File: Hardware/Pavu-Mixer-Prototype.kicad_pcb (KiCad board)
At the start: 2 copper layers, 155.9 x 91.9 mm, 65 parts, among them J1 Conn_02x16_Counter_Clockwise, U1 74HC595, U2 74HC595, U3 74HC595, U4 PCA9555D, U5 PCA9536D

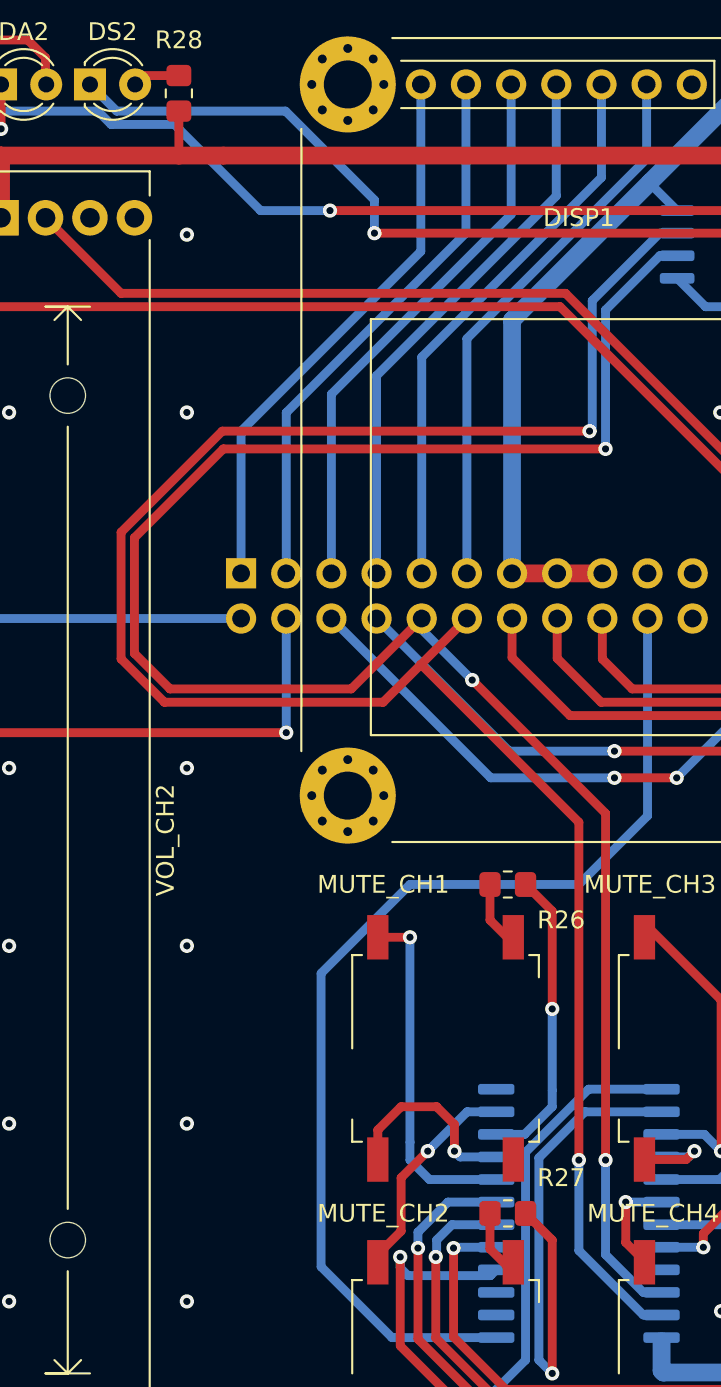
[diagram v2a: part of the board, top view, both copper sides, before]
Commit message: Cleanup some tracks
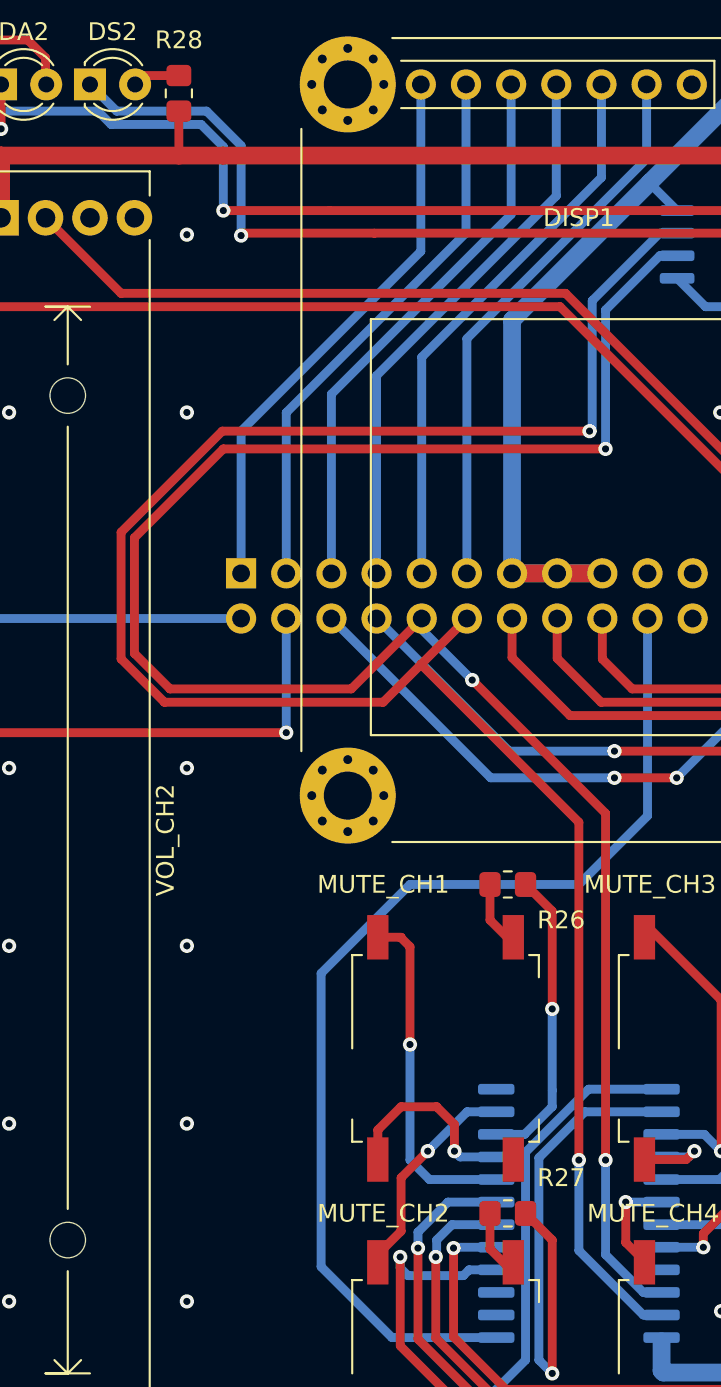
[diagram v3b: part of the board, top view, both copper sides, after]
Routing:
- net +3V3: track 456.7 -> 462.0 mm
- net /DESYNC_CH1: track 60.3 -> 62.4 mm
- net /DESYNC_CH2: track 46.6 -> 48.6 mm
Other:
- board text added: "Pavu-Mixer Rev 1.0 2021-03-29 Rahix"
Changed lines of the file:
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@@
   (general
     (thickness 1.6)
-    (drawings 6)
-    (tracks 642)
+    (drawings 7)
+    (tracks 649)
     (zones 0)
     (modules 65)
@@
     (tags "SOIC SO")
     (attr smd)
-    (fp_text reference U5 (at 0 3.4) (layer B.SilkS)
+    (fp_text reference U5 (at 0 3.5) (layer B.SilkS)
       (effects (font (size 1 1) (thickness 0.15)) (justify mirror))
     )
@@
     (tags "SOIC SO")
     (attr smd)
-    (fp_text reference U4 (at 0 8.65) (layer B.SilkS)
+    (fp_text reference U4 (at 0.5 9) (layer B.SilkS)
       (effects (font (size 1 1) (thickness 0.15)) (justify mirror))
     )
@@
     (tags "SOIC SO")
     (attr smd)
-    (fp_text reference U3 (at 0 5.9) (layer B.SilkS)
+    (fp_text reference U3 (at 1.5 6) (layer B.SilkS)
       (effects (font (size 1 1) (thickness 0.15)) (justify mirror))
     )
@@
     (tags "SOIC SO")
     (attr smd)
-    (fp_text reference U2 (at 0 5.9) (layer B.SilkS)
+    (fp_text reference U2 (at 1.5 6) (layer B.SilkS)
       (effects (font (size 1 1) (thickness 0.15)) (justify mirror))
     )
@@
     (tags "SOIC SO")
     (attr smd)
-    (fp_text reference U1 (at 0 5.9) (layer B.SilkS)
+    (fp_text reference U1 (at 1.5 6) (layer B.SilkS)
       (effects (font (size 1 1) (thickness 0.15)) (justify mirror))
     )
@@
     (descr "Through hole straight pin header, 2x16, 2.54mm pitch, double rows")
     (tags "Through hole pin header THT 2x16 2.54mm double row")
-    (fp_text reference J1 (at 1.27 2.33 90) (layer B.SilkS)
+    (fp_text reference J1 (at 0 3 180) (layer B.SilkS)
       (effects (font (size 1 1) (thickness 0.15)) (justify mirror))
     )
@@
     )
   )
+  (gr_text "Pavu-Mixer Rev 1.0\n2021-03-29  Rahix" (at 92.5 106) (layer B.SilkS)
+    (effects (font (size 2 2) (thickness 0.15)) (justify mirror))
+  )
   (dimension 155.9 (width 0.15) (layer Dwgs.User)
     (gr_text "155.900 mm" (at 147.95 152.2) (layer Dwgs.User)
@@
   (segment (start 159.05 120.4) (end 144.5 134.95) (width 1) (layer B.Cu) (net 52))
   (segment (start 180.5 120.4) (end 159.05 120.4) (width 1) (layer B.Cu) (net 52))
+  (segment (start 126.24 90) (end 131.5 90) (width 1) (layer B.Cu) (net 52))
   (segment (start 126.19 69.81) (end 126.19 62.5) (width 0.5) (layer B.Cu) (net 53))
   (segment (start 116.08 79.92) (end 126.19 69.81) (width 0.5) (layer B.Cu) (net 53))
@@
   (via (at 142.5 69.595) (size 0.8) (drill 0.4) (layers F.Cu B.Cu) (net 58))
   (segment (start 142.5 69.595) (end 116 69.595) (width 0.5) (layer F.Cu) (net 58))
-  (via (at 116 69.595) (size 0.8) (drill 0.4) (layers F.Cu B.Cu) (net 58))
-  (segment (start 112.095 69.595) (end 116 69.595) (width 0.5) (layer B.Cu) (net 58))
-  (segment (start 107.25001 64.75001) (end 112.095 69.595) (width 0.5) (layer B.Cu) (net 58))
+  (segment (start 116 69.595) (end 110 69.595) (width 0.5) (layer F.Cu) (net 58))
+  (via (at 110 69.595) (size 0.8) (drill 0.4) (layers F.Cu B.Cu) (net 58))
+  (segment (start 108.75001 64.75001) (end 110 66) (width 0.5) (layer B.Cu) (net 58))
+  (segment (start 110 66) (end 110 69.595) (width 0.5) (layer B.Cu) (net 58))
+  (segment (start 103.689336 64.75001) (end 108.75001 64.75001) (width 0.5) (layer B.Cu) (net 58))
   (segment (start 102.939326 64) (end 103.689336 64.75001) (width 0.5) (layer B.Cu) (net 58))
   (segment (start 88.5 64) (end 102.939326 64) (width 0.5) (layer B.Cu) (net 58))
   (segment (start 87.5 63) (end 88.5 64) (width 0.5) (layer B.Cu) (net 58))
-  (segment (start 103.689336 64.75001) (end 107.25001 64.75001) (width 0.5) (layer B.Cu) (net 58))
   (segment (start 87.5 62.5) (end 87.5 63) (width 0.5) (layer B.Cu) (net 58))
   (segment (start 105.5 62) (end 105 62.5) (width 0.5) (layer F.Cu) (net 59))
@@
   (via (at 142.5 70.865) (size 0.8) (drill 0.4) (layers F.Cu B.Cu) (net 60))
   (segment (start 142.5 70.865) (end 118.5 70.865) (width 0.5) (layer F.Cu) (net 60))
-  (via (at 118.5 70.865) (size 0.8) (drill 0.4) (layers F.Cu B.Cu) (net 60))
-  (segment (start 118.5 70.865) (end 118.5 69) (width 0.5) (layer B.Cu) (net 60))
-  (segment (start 118.5 69) (end 113.5 64) (width 0.5) (layer B.Cu) (net 60))
-  (segment (start 113.5 64) (end 104 64) (width 0.5) (layer B.Cu) (net 60))
   (segment (start 104 64) (end 102.5 62.5) (width 0.5) (layer B.Cu) (net 60))
+  (segment (start 109.060675 64.000001) (end 111 65.939326) (width 0.5) (layer B.Cu) (net 60))
+  (segment (start 104 64) (end 109.060675 64.000001) (width 0.5) (layer B.Cu) (net 60))
+  (via (at 111 71) (size 0.8) (drill 0.4) (layers F.Cu B.Cu) (net 60))
+  (segment (start 111.135 70.865) (end 111 71) (width 0.5) (layer F.Cu) (net 60))
+  (segment (start 118.5 70.865) (end 111.135 70.865) (width 0.5) (layer F.Cu) (net 60))
+  (segment (start 111 71) (end 111 65.939326) (width 0.5) (layer B.Cu) (net 60))
   (segment (start 165 62) (end 163 62) (width 0.5) (layer F.Cu) (net 61))
   (segment (start 163 62) (end 162.5 62.5) (width 0.5) (layer F.Cu) (net 61))
@@
   (via (at 119.95 128.45) (size 0.8) (drill 0.4) (layers F.Cu B.Cu) (net 66))
   (segment (start 119.949997 129.065685) (end 120.384312 129.5) (width 0.5) (layer B.Cu) (net 66))
-  (segment (start 125.025 129.5) (end 120.384312 129.5) (width 0.5) (layer B.Cu) (net 66))
-  (segment (start 125.35 129.175) (end 125.025 129.5) (width 0.5) (layer B.Cu) (net 66))
   (segment (start 147.9 138.5) (end 147.95 138.45) (width 0.5) (layer F.Cu) (net 66))
   (segment (start 120 133.5) (end 125 138.5) (width 0.5) (layer F.Cu) (net 66))
@@
   (segment (start 119.949997 129.065685) (end 119.949997 128.450003) (width 0.5) (layer B.Cu) (net 66))
   (segment (start 119.95 128.45) (end 119.95 133.45) (width 0.5) (layer F.Cu) (net 66))
+  (segment (start 125.35 129.175) (end 123.825 129.175) (width 0.5) (layer B.Cu) (net 66))
+  (segment (start 123.5 129.5) (end 120.384312 129.5) (width 0.5) (layer B.Cu) (net 66))
+  (segment (start 123.825 129.175) (end 123.5 129.5) (width 0.5) (layer B.Cu) (net 66))
   (segment (start 134.55 72.135) (end 131.5 75.185) (width 0.5) (layer B.Cu) (net 67))
   (segment (start 135.525 72.135) (end 134.55 72.135) (width 0.5) (layer B.Cu) (net 67))
@@
   (segment (start 123.325 122.825) (end 123 122.5) (width 0.5) (layer B.Cu) (net 78))
   (segment (start 125.35 122.825) (end 123.325 122.825) (width 0.5) (layer B.Cu) (net 78))
-  (segment (start 118.69 110.469) (end 120.5 110.469) (width 0.5) (layer F.Cu) (net 79))
-  (via (at 120.5 110.469) (size 0.8) (drill 0.4) (layers F.Cu B.Cu) (net 79))
-  (segment (start 120.5 110.469) (end 120.5 122) (width 0.5) (layer B.Cu) (net 79))
-  (segment (start 125.35 124.095) (end 121.595 124.095) (width 0.5) (layer B.Cu) (net 79))
-  (segment (start 120.5 123) (end 120.5 122) (width 0.5) (layer B.Cu) (net 79))
-  (segment (start 121.595 124.095) (end 120.5 123) (width 0.5) (layer B.Cu) (net 79))
+  (segment (start 118.69 110.469) (end 120 110.469) (width 0.5) (layer F.Cu) (net 79))
+  (segment (start 120 110.469) (end 120 110.5) (width 0.5) (layer F.Cu) (net 79))
+  (segment (start 120 110.5) (end 120.5 111) (width 0.5) (layer F.Cu) (net 79))
+  (segment (start 120.5 111) (end 120.5 116.5) (width 0.5) (layer F.Cu) (net 79))
+  (via (at 120.5 116.5) (size 0.8) (drill 0.4) (layers F.Cu B.Cu) (net 79))
+  (segment (start 121.595 124.095) (end 125.35 124.095) (width 0.5) (layer B.Cu) (net 79))
+  (segment (start 120.5 123) (end 121.595 124.095) (width 0.5) (layer B.Cu) (net 79))
+  (segment (start 120.5 116.5) (end 120.5 123) (width 0.5) (layer B.Cu) (net 79))
   (segment (start 125 107.5) (end 125 109.5) (width 0.5) (layer F.Cu) (net 80))
   (segment (start 125 109.5) (end 126 110.5) (width 0.5) (layer F.Cu) (net 80))

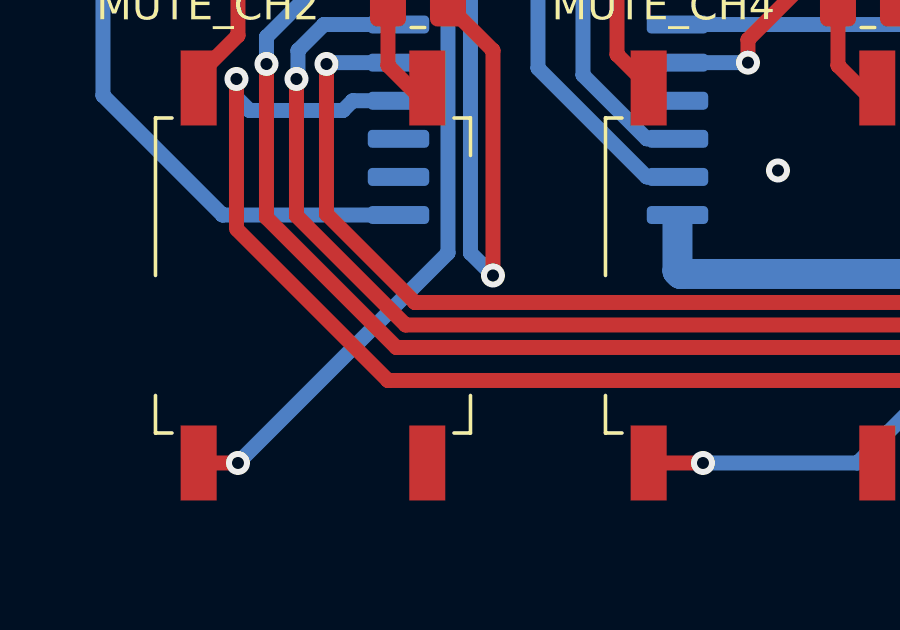
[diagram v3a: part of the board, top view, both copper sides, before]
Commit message: Add pull-up for PCA_INT signal
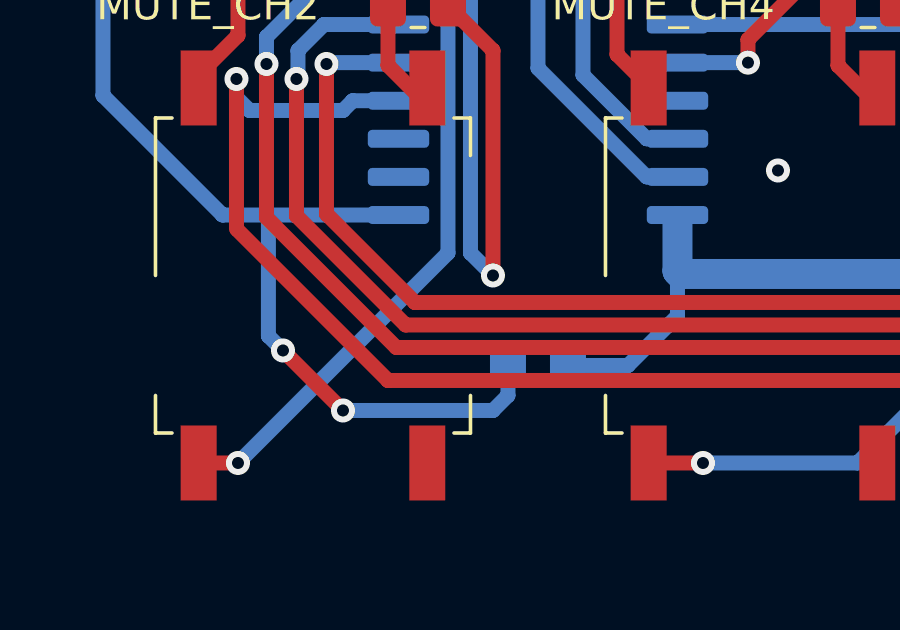
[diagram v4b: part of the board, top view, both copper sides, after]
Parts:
- added R35: 10k, Resistor_SMD:R_0805_2012Metric_Pad1.20x1.40mm_HandSolder, B.Cu at (130.0, 138.0)
- J1: value Conn_02x16_Counter_Clockwise -> Conn_02x16_Odd_Even
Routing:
- net PCA_INT: track 61.1 -> 75.4 mm, vias 0 -> 2
- net +3V3: track 462.0 -> 467.8 mm
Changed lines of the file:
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@@
     (thickness 1.6)
     (drawings 7)
-    (tracks 649)
+    (tracks 661)
     (zones 0)
-    (modules 65)
+    (modules 66)
     (nets 100)
   )
@@
     (add_net "Net-(MUTE_MAIN1-Pad3)")
     (add_net "Net-(U1-Pad14)")
+    (add_net "Net-(U1-Pad4)")
+    (add_net "Net-(U1-Pad5)")
+    (add_net "Net-(U1-Pad6)")
+    (add_net "Net-(U1-Pad7)")
+    (add_net "Net-(U1-Pad9)")
     (add_net "Net-(U2-Pad14)")
+    (add_net "Net-(VOL_CH1-Pad4)")
+    (add_net "Net-(VOL_CH1-Pad5)")
+    (add_net "Net-(VOL_CH1-Pad6)")
+    (add_net "Net-(VOL_CH2-Pad4)")
+    (add_net "Net-(VOL_CH2-Pad5)")
+    (add_net "Net-(VOL_CH2-Pad6)")
+    (add_net "Net-(VOL_CH3-Pad4)")
+    (add_net "Net-(VOL_CH3-Pad5)")
+    (add_net "Net-(VOL_CH3-Pad6)")
+    (add_net "Net-(VOL_CH4-Pad4)")
+    (add_net "Net-(VOL_CH4-Pad5)")
+    (add_net "Net-(VOL_CH4-Pad6)")
+    (add_net "Net-(VOL_MAIN1-Pad4)")
+    (add_net "Net-(VOL_MAIN1-Pad5)")
+    (add_net "Net-(VOL_MAIN1-Pad6)")
     (add_net PCA_INT)
     (add_net VOL1)
@@
     (diff_pair_gap 0.12)
   )
+  (module Resistor_SMD:R_0805_2012Metric_Pad1.20x1.40mm_HandSolder (layer B.Cu)
+    (at 130 138 180)
+    (descr "Resistor SMD 0805 (2012 Metric), square (rectangular) end terminal, IPC_7351 nominal with elongated pad for handsoldering. (Body size source: IPC-SM-782 page 72, https://www.pcb-3d.com/wordpress/wp-content/uploads/ipc-sm-782a_amendment_1_and_2.pdf), generated with kicad-footprint-generator")
+    (tags "resistor handsolder")
+    (attr smd)
+    (fp_text reference R35 (at 0 -2) (layer B.SilkS)
+      (effects (font (size 1 1) (thickness 0.15)) (justify mirror))
+    )
+    (fp_text value 10k (at 0 1.5) (layer B.Fab)
+      (effects (font (size 1 1) (thickness 0.15)) (justify mirror))
+    )
+    (fp_text user %R (at 0 0) (layer B.Fab)
+      (effects (font (size 0.5 0.5) (thickness 0.08)) (justify mirror))
+    )
+    (fp_line (start -1 -0.625) (end -1 0.625) (layer B.Fab) (width 0.1))
+    (fp_line (start -1 0.625) (end 1 0.625) (layer B.Fab) (width 0.1))
+    (fp_line (start 1 0.625) (end 1 -0.625) (layer B.Fab) (width 0.1))
+    (fp_line (start 1 -0.625) (end -1 -0.625) (layer B.Fab) (width 0.1))
+    (fp_line (start -0.227064 0.735) (end 0.227064 0.735) (layer B.SilkS) (width 0.12))
+    (fp_line (start -0.227064 -0.735) (end 0.227064 -0.735) (layer B.SilkS) (width 0.12))
+    (fp_line (start -1.85 -0.95) (end -1.85 0.95) (layer B.CrtYd) (width 0.05))
+    (fp_line (start -1.85 0.95) (end 1.85 0.95) (layer B.CrtYd) (width 0.05))
+    (fp_line (start 1.85 0.95) (end 1.85 -0.95) (layer B.CrtYd) (width 0.05))
+    (fp_line (start 1.85 -0.95) (end -1.85 -0.95) (layer B.CrtYd) (width 0.05))
+    (pad 2 smd roundrect (at 1 0 180) (size 1.2 1.4) (layers B.Cu B.Paste B.Mask) (roundrect_rratio 0.208333)
+      (net 72 PCA_INT))
+    (pad 1 smd roundrect (at -1 0 180) (size 1.2 1.4) (layers B.Cu B.Paste B.Mask) (roundrect_rratio 0.208333)
+      (net 52 +3V3))
+    (model ${KISYS3DMOD}/Resistor_SMD.3dshapes/R_0805_2012Metric.wrl
+      (at (xyz 0 0 0))
+      (scale (xyz 1 1 1))
+      (rotate (xyz 0 0 0))
+    )
+  )
   (module Package_SO:SOIC-8_3.9x4.9mm_P1.27mm (layer B.Cu)
     (at 138 71.5 180)
@@
       (effects (font (size 1 1) (thickness 0.15)) (justify mirror))
     )
-    (fp_text value Conn_02x16_Counter_Clockwise (at 1.27 -40.43 90) (layer B.Fab)
+    (fp_text value Conn_02x16_Odd_Even (at 1.27 -40.43 90) (layer B.Fab)
       (effects (font (size 1 1) (thickness 0.15)) (justify mirror))
     )
@@
   (segment (start 180.5 120.4) (end 159.05 120.4) (width 1) (layer B.Cu) (net 52))
   (segment (start 126.24 90) (end 131.5 90) (width 1) (layer B.Cu) (net 52))
+  (segment (start 134.65 134.85) (end 134.65 136.35) (width 0.5) (layer B.Cu) (net 52))
+  (segment (start 134.65 136.35) (end 133 138) (width 0.5) (layer B.Cu) (net 52))
+  (segment (start 133 138) (end 131 138) (width 0.5) (layer B.Cu) (net 52))
   (segment (start 126.19 69.81) (end 126.19 62.5) (width 0.5) (layer B.Cu) (net 53))
   (segment (start 116.08 79.92) (end 126.19 69.81) (width 0.5) (layer B.Cu) (net 53))
@@
   (segment (start 115.5 112.5) (end 115.5 129) (width 0.5) (layer B.Cu) (net 72))
   (segment (start 119.485 132.985) (end 115.5 129) (width 0.5) (layer B.Cu) (net 72))
-  (segment (start 125.35 132.985) (end 119.485 132.985) (width 0.5) (layer B.Cu) (net 72))
+  (via (at 121.5 137.5) (size 0.8) (drill 0.4) (layers F.Cu B.Cu) (net 72))
+  (segment (start 121.015 137.015) (end 121.5 137.5) (width 0.5) (layer B.Cu) (net 72))
+  (segment (start 121.015 132.985) (end 121.015 137.015) (width 0.5) (layer B.Cu) (net 72))
+  (segment (start 125.35 132.985) (end 121.015 132.985) (width 0.5) (layer B.Cu) (net 72))
+  (segment (start 121.015 132.985) (end 119.485 132.985) (width 0.5) (layer B.Cu) (net 72))
+  (via (at 123.5 139.5) (size 0.8) (drill 0.4) (layers F.Cu B.Cu) (net 72))
+  (segment (start 121.5 137.5) (end 123.5 139.5) (width 0.5) (layer F.Cu) (net 72))
+  (segment (start 129 138) (end 129 139) (width 0.5) (layer B.Cu) (net 72))
+  (segment (start 128.5 139.5) (end 123.5 139.5) (width 0.5) (layer B.Cu) (net 72))
+  (segment (start 129 139) (end 128.5 139.5) (width 0.5) (layer B.Cu) (net 72))
   (segment (start 210 68.585787) (end 208.414213 67) (width 0.5) (layer B.Cu) (net 73))
   (segment (start 210 70) (end 210 68.585787) (width 0.5) (layer B.Cu) (net 73))

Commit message: LED Series resistors 100 ohm instead of 47
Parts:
- R1, R10, R11, R12, R13, R14, R15, R16, R17, R18, R19, R2, R20, R21, R22, R23, R24, R25, R26, R27, R28, R29, R3, R30, R31, R32, R33, R34, R4, R5, R6, R7, R8, R9: value 47 -> 100
